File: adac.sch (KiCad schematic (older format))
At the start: 21 parts

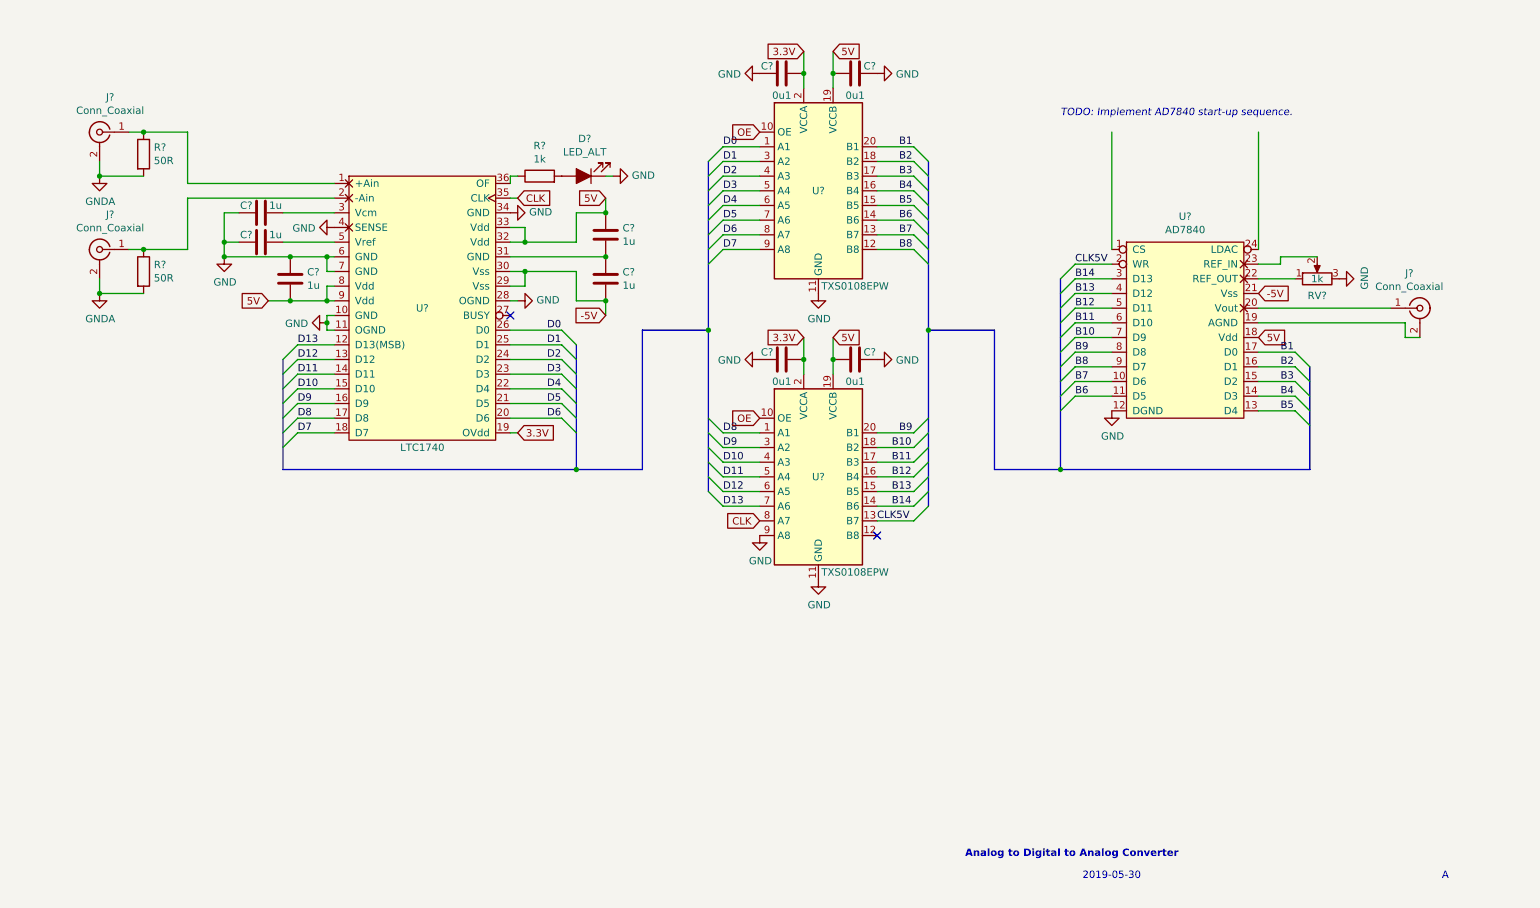
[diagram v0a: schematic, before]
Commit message: Rev A complete
Added initialization for the DAC and other minor changes.
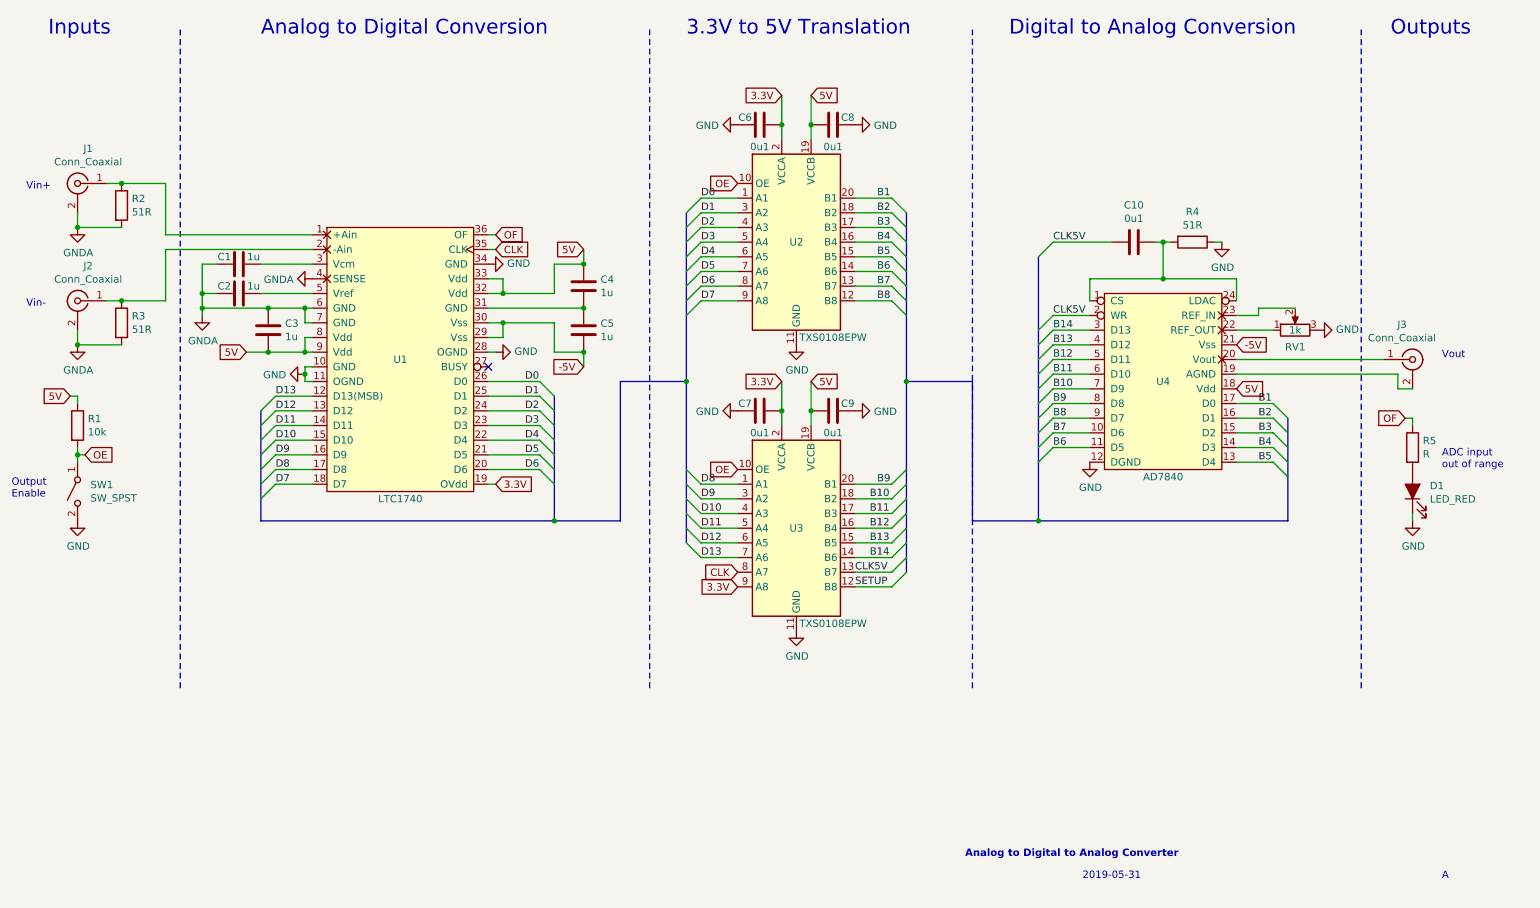
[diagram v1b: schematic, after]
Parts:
- removed D?: LED_ALT, symbol Device:LED_ALT
- removed R?: 1k, symbol Device:R
- added C10: 0u1, symbol Device:C
- added D1: LED_RED, symbol Device:LED_ALT
- added R1: 10k, symbol Device:R
- added R4: 51R, symbol Device:R
- added R5: R, symbol Device:R
- added SW1: SW_SPST, symbol Switch:SW_SPST
- R2, R3: renamed from R?; value 50R -> 51R
- gave numbers to parts that had none: 17
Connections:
- net 3.3V: now also U3.9 (A8)
- net 5V: now also R1.1
- net CLK5V: now also C10.2
- net GND: now also D1.1 (K), R4.1, SW1.2 (B); no longer C1.2, C2.2, C3.1, U1.4 (SENSE), U1.6 (GND), U1.7 (GND), U3.9 (A8)
- net GNDA: now also C1.2, C2.2, C3.1, U1.4 (SENSE), U1.6 (GND), U1.7 (GND)
- net OE: now also R1.2, SW1.1 (A)
- net OF: now reaches U1.36 (OF)
- net OF: now also R5.1
- net SETUP: now reaches U3.12 (B8)
- net at U4.1 (CS): now also U4.24 (LDAC), C10.1, R4.2
- new net: D1.2 (A), R5.2
- no-connect marks 2 -> 1
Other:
- note added: "2019-05-31"
- note added: "3.3V to 5V Translation"
- note added: "ADC input\nout of range"
- note added: "Analog to Digital Conversion"
- note added: "Digital to Analog Conversion"
- note added: "Inputs"
- note added: "Output\nEnable"
- note added: "Outputs"
- note added: "Vin+"
- note added: "Vin-"
- note added: "Vout"
- note removed: "2019-05-30"
- note removed: "TODO: Implement AD7840 start-up sequence."
- moved on the sheet: C1, C2, C3, C4, C5, C6, C7, C8, C9, J1, J2, J3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

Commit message: Added power flags to pass ERC
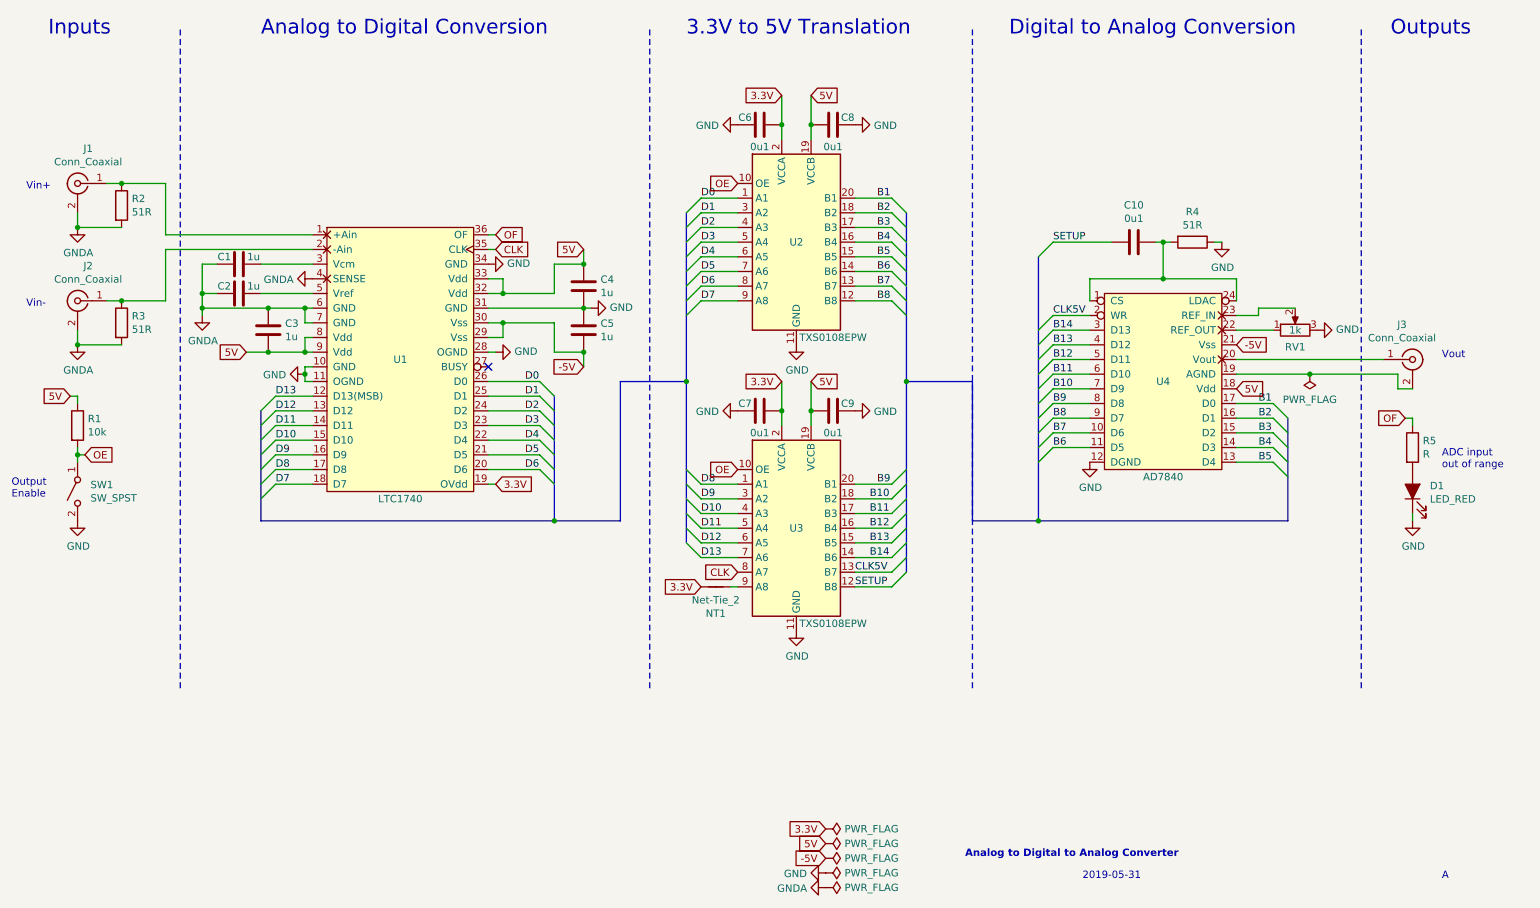
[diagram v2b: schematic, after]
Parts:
- added NT1: Net-Tie_2, symbol Device:Net-Tie_2
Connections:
- net 3.3V: now also NT1.2; no longer U3.9 (A8)
- net CLK5V: no longer C10.2
- net GND: now also C4.2, C5.1, U1.31 (GND)
- net SETUP: now also C10.2
- new net: NT1.1, U3.9 (A8)
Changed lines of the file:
@@
 Wire Wire Line
 	2550 3650 2900 3650
-Wire Wire Line
-	2150 3750 2600 3750
 Connection ~ 2600 3750
 Text GLabel 2450 4050 0    50   Input ~ 0
@@
 Connection ~ 4750 3450
 $Comp
-L power:GND #PWR011
+L power:GND #PWR012
 U 1 1 5CF89283
 P 6200 4000
-F 0 "#PWR011" H 6200 3750 50  0001 C CNN
+F 0 "#PWR012" H 6200 3750 50  0001 C CNN
 F 1 "GND" H 6205 3827 50  0000 C CNN
 F 2 "" H 6200 4000 50  0001 C CNN
@@
 5V
 $Comp
-L power:GND #PWR09
+L power:GND #PWR010
 U 1 1 5D00A6EA
 P 5800 2500
-F 0 "#PWR09" H 5800 2250 50  0001 C CNN
+F 0 "#PWR010" H 5800 2250 50  0001 C CNN
 F 1 "GND" V 5805 2372 50  0000 R CNN
 F 2 "" H 5800 2500 50  0001 C CNN
@@
 $EndComp
 $Comp
-L power:GND #PWR013
+L power:GND #PWR016
 U 1 1 5D0181CF
 P 6600 2500
-F 0 "#PWR013" H 6600 2250 50  0001 C CNN
+F 0 "#PWR016" H 6600 2250 50  0001 C CNN
 F 1 "GND" V 6605 2372 50  0000 R CNN
 F 2 "" H 6600 2500 50  0001 C CNN
@@
 	6300 2500 6300 2600
 $Comp
-L power:GND #PWR012
+L power:GND #PWR013
 U 1 1 5D02ED9B
 P 6200 5950
-F 0 "#PWR012" H 6200 5700 50  0001 C CNN
+F 0 "#PWR013" H 6200 5700 50  0001 C CNN
 F 1 "GND" H 6205 5777 50  0000 C CNN
 F 2 "" H 6200 5950 50  0001 C CNN
@@
 3.3V
 $Comp
-L power:GND #PWR010
+L power:GND #PWR011
 U 1 1 5D02EDC2
 P 5800 4450
-F 0 "#PWR010" H 5800 4200 50  0001 C CNN
+F 0 "#PWR011" H 5800 4200 50  0001 C CNN
 F 1 "GND" V 5805 4322 50  0000 R CNN
 F 2 "" H 5800 4450 50  0001 C CNN
@@
 $EndComp
 $Comp
-L power:GND #PWR014
+L power:GND #PWR017
 U 1 1 5D02EDD1
 P 6600 4450
-F 0 "#PWR014" H 6600 4200 50  0001 C CNN
+F 0 "#PWR017" H 6600 4200 50  0001 C CNN
 F 1 "GND" V 6605 4322 50  0000 R CNN
 F 2 "" H 6600 4450 50  0001 C CNN
@@
 Wire Wire Line
 	6600 5450 6850 5450
-Entry Wire Line
-	6850 5550 6950 5450
 Wire Wire Line
 	6600 5550 6850 5550
@@
 	7400 4250 7400 5200
 $Comp
-L power:GND #PWR015
+L power:GND #PWR018
 U 1 1 5D1BFBF2
 P 8200 4800
-F 0 "#PWR015" H 8200 4550 50  0001 C CNN
+F 0 "#PWR018" H 8200 4550 50  0001 C CNN
 F 1 "GND" H 8205 4627 50  0000 C CNN
 F 2 "" H 8200 4800 50  0001 C CNN
@@
 B14
 Entry Wire Line
-	6850 5650 6950 5550
-Wire Wire Line
-	6600 5650 6850 5650
-Text Label 6600 5650 0    50   ~ 0
-SETUP
-Text GLabel 5800 5650 0    50   Input ~ 0
-3.3V
-Entry Wire Line
 	7850 3400 7950 3300
 $Comp
@@
 $EndComp
 $Comp
-L power:GND #PWR016
+L power:GND #PWR019
 U 1 1 5CFA5CCE
 P 9100 3300
-F 0 "#PWR016" H 9100 3050 50  0001 C CNN
+F 0 "#PWR019" H 9100 3050 50  0001 C CNN
 F 1 "GND" H 9105 3127 50  0000 C CNN
 F 2 "" H 9100 3300 50  0001 C CNN
@@
 $EndComp
 Text Label 7950 3300 0    50   ~ 0
-CLK5V
+SETUP
 Connection ~ 7850 5200
 Wire Bus Line
@@
 $EndComp
 $Comp
-L power:GND #PWR017
+L power:GND #PWR020
 U 1 1 5D028740
 P 9750 3900
-F 0 "#PWR017" H 9750 3650 50  0001 C CNN
+F 0 "#PWR020" H 9750 3650 50  0001 C CNN
 F 1 "GND" V 9755 3772 50  0000 R CNN
 F 2 "" H 9750 3900 50  0001 C CNN
@@
 	9200 4100 10200 4100
 Wire Wire Line
-	9200 4200 10300 4200
+	9200 4200 9700 4200
 Text GLabel 6100 2300 0    50   Input ~ 0
 3.3V
@@
 $EndComp
 $Comp
-L power:GND #PWR018
+L power:GND #PWR021
 U 1 1 5D1BDCD3
 P 10400 5200
-F 0 "#PWR018" H 10400 4950 50  0001 C CNN
+F 0 "#PWR021" H 10400 4950 50  0001 C CNN
 F 1 "GND" H 10405 5027 50  0000 C CNN
 F 2 "" H 10400 5200 50  0001 C CNN
@@
 Wire Wire Line
 	2150 3750 2150 3800
+Entry Wire Line
+	6850 5550 6950 5450
+Wire Wire Line
+	2150 3750 2600 3750
+Text GLabel 6400 7400 0    50   Input ~ 0
+5V
+Text GLabel 6400 7500 0    50   Input ~ 0
+-5V
+Text GLabel 6400 7300 0    50   Input ~ 0
+3.3V
+$Comp
+L power:PWR_FLAG #FLG01
+U 1 1 5CF5C463
+P 6400 7300
+F 0 "#FLG01" H 6400 7375 50  0001 C CNN
+F 1 "PWR_FLAG" V 6400 7428 50  0000 L CNN
+F 2 "" H 6400 7300 50  0001 C CNN
+F 3 "~" H 6400 7300 50  0001 C CNN
+	1    6400 7300
+	0    1    1    0
+$EndComp
+$Comp
+L power:PWR_FLAG #FLG02
+U 1 1 5CF5CD86
+P 6400 7400
+F 0 "#FLG02" H 6400 7475 50  0001 C CNN
+F 1 "PWR_FLAG" V 6400 7528 50  0000 L CNN
+F 2 "" H 6400 7400 50  0001 C CNN
+F 3 "~" H 6400 7400 50  0001 C CNN
+	1    6400 7400
+	0    1    1    0
+$EndComp
+$Comp
+L power:PWR_FLAG #FLG03
+U 1 1 5CF5CFB9
+P 6400 7500
+F 0 "#FLG03" H 6400 7575 50  0001 C CNN
+F 1 "PWR_FLAG" V 6400 7628 50  0000 L CNN
+F 2 "" H 6400 7500 50  0001 C CNN
+F 3 "~" H 6400 7500 50  0001 C CNN
+	1    6400 7500
+	0    1    1    0
+$EndComp
+$Comp
+L power:PWR_FLAG #FLG06
+U 1 1 5CF5D471
+P 9700 4200
+F 0 "#FLG06" H 9700 4275 50  0001 C CNN
+F 1 "PWR_FLAG" H 9700 4373 50  0000 C CNN
+F 2 "" H 9700 4200 50  0001 C CNN
+F 3 "~" H 9700 4200 50  0001 C CNN
+	1    9700 4200
+	-1   0    0    1
+$EndComp
+Connection ~ 9700 4200
+Wire Wire Line
+	9700 4200 10300 4200
+$Comp
+L power:GND #PWR09
+U 1 1 5CF5F6BA
+P 4800 3750
+F 0 "#PWR09" H 4800 3500 50  0001 C CNN
+F 1 "GND" V 4805 3622 50  0000 R CNN
+F 2 "" H 4800 3750 50  0001 C CNN
+F 3 "" H 4800 3750 50  0001 C CNN
+	1    4800 3750
+	0    -1   -1   0
+$EndComp
+Wire Wire Line
+	4750 3750 4800 3750
+Wire Wire Line
+	6600 5650 6850 5650
+Entry Wire Line
+	6850 5650 6950 5550
+Text Label 6600 5650 0    50   ~ 0
+SETUP
+$Comp
+L power:PWR_FLAG #FLG05
+U 1 1 5CF5F38F
+P 6400 7700
+F 0 "#FLG05" H 6400 7775 50  0001 C CNN
+F 1 "PWR_FLAG" V 6400 7828 50  0000 L CNN
+F 2 "" H 6400 7700 50  0001 C CNN
+F 3 "~" H 6400 7700 50  0001 C CNN
+	1    6400 7700
+	0    1    1    0
+$EndComp
+$Comp
+L power:GNDA #PWR015
+U 1 1 5CF5ED2B
+P 6400 7700
+F 0 "#PWR015" H 6400 7450 50  0001 C CNN
+F 1 "GNDA" V 6405 7573 50  0000 R CNN
+F 2 "" H 6400 7700 50  0001 C CNN
+F 3 "" H 6400 7700 50  0001 C CNN
+	1    6400 7700
+	0    1    1    0
+$EndComp
+$Comp
+L power:PWR_FLAG #FLG04
+U 1 1 5CF5F1F9
+P 6400 7600
+F 0 "#FLG04" H 6400 7675 50  0001 C CNN
+F 1 "PWR_FLAG" V 6400 7728 50  0000 L CNN
+F 2 "" H 6400 7600 50  0001 C CNN
+F 3 "~" H 6400 7600 50  0001 C CNN
+	1    6400 7600
+	0    1    1    0
+$EndComp
+$Comp
+L power:GND #PWR014
+U 1 1 5CF5E2AE
+P 6400 7600
+F 0 "#PWR014" H 6400 7350 50  0001 C CNN
+F 1 "GND" V 6405 7472 50  0000 R CNN
+F 2 "" H 6400 7600 50  0001 C CNN
+F 3 "" H 6400 7600 50  0001 C CNN
+	1    6400 7600
+	0    1    1    0
+$EndComp
+$Comp
+L Device:Net-Tie_2 NT1
+U 1 1 5CFEEC9B
+P 5650 5650
+F 0 "NT1" H 5650 5831 50  0000 C CNN
+F 1 "Net-Tie_2" H 5650 5740 50  0000 C CNN
+F 2 "" H 5650 5650 50  0001 C CNN
+F 3 "~" H 5650 5650 50  0001 C CNN
+	1    5650 5650
+	-1   0    0    1
+$EndComp
+Wire Wire Line
+	5800 5650 5750 5650
+Text GLabel 5550 5650 0    50   Input ~ 0
+3.3V
 Wire Bus Line
 	9550 4500 9550 5200
